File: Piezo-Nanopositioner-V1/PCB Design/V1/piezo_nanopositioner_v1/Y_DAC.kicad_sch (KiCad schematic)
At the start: 29 parts, among them J6 Conn_01x10_Pin, J7 RF2-04A-T-00-50-G, U7 TL431AIDBZR, U8 DAC0800LCM, U9 TDA2050

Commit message: started PCB design, almost finished first DAC.
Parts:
- removed J7: RF2-04A-T-00-50-G, RF:CONN_RF2-04A-T-00-50-G_ADM, symbol SMA_Connector:RF2-04A-T-00-50-G
- added J3: RF2-04A-T-00-50-G, CONN_RF2-04A-T-00-50-G_ADM, symbol SMA_Connector:RF2-04A-T-00-50-G
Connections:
- net at C29.2, R38.2, R39.1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: now also J3.1 (Sig)
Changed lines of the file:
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@@
-	)
-	(symbol
-		(lib_id "SMA_Connector:RF2-04A-T-00-50-G")
-		(at 224.79 101.6 0)
-		(unit 1)
-		(exclude_from_sim no)
-		(in_bom yes)
-		(on_board yes)
-		(dnp no)
-		(fields_autoplaced yes)
-		(property "Reference" "J7"
-			(at 238.76 100.3299 0)
-			(effects
-				(font
-					(size 1.524 1.524)
-				)
-				(justify left)
-			)
-		)
-		(property "Value" "RF2-04A-T-00-50-G"
-			(at 238.76 102.8699 0)
-			(effects
-				(font
-					(size 1.524 1.524)
-				)
-				(justify left)
-			)
-		)
-		(property "Footprint" "RF:CONN_RF2-04A-T-00-50-G_ADM"
-			(at 224.79 101.6 0)
-			(effects
-				(font
-					(size 1.27 1.27)
-					(italic yes)
-				)
-				(hide yes)
-			)
-		)
-		(property "Datasheet" "RF2-04A-T-00-50-G"
-			(at 224.79 101.6 0)
-			(effects
-				(font
-					(size 1.27 1.27)
-					(italic yes)
-				)
-				(hide yes)
-			)
-		)
-		(property "Description" ""
-			(at 224.79 101.6 0)
-			(effects
-				(font
-					(size 1.27 1.27)
-				)
-				(hide yes)
-			)
-		)
-		(pin "1"
-		)
-		(instances
-			(project "piezo_nanopositioner_v1"
-				(path "/7b2a32d8-cc7d-471d-a8eb-eea62713ed45/2b7af091-9ff3-4afc-ada8-05e74516fa9c"
-					(reference "J7")
-					(unit 1)
-				)
-			)
-		)
 	)
 	(symbol
@@
 					(unit 1)
 				)
+			)
+		)
+	)
+	(symbol
+		(lib_id "SMA_Connector:RF2-04A-T-00-50-G")
+		(at 224.79 101.6 0)
+		(unit 1)
+		(exclude_from_sim no)
+		(in_bom yes)
+		(on_board yes)
+		(dnp no)
+		(fields_autoplaced yes)
+		(property "Reference" "J3"
+			(at 238.76 100.3299 0)
+			(effects
+				(font
+					(size 1.524 1.524)
+				)
+				(justify left)
+			)
+		)
+		(property "Value" "RF2-04A-T-00-50-G"
+			(at 238.76 102.8699 0)
+			(effects
+				(font
+					(size 1.524 1.524)
+				)
+				(justify left)
+			)
+		)
+		(property "Footprint" "CONN_RF2-04A-T-00-50-G_ADM"
+			(at 225.552 92.456 0)
+			(effects
+				(font
+					(size 1.27 1.27)
+					(italic yes)
+				)
+				(hide yes)
+			)
+		)
+		(property "Datasheet" "RF2-04A-T-00-50-G"
+			(at 217.17 104.394 0)
+			(effects
+				(font
+					(size 1.27 1.27)
+					(italic yes)
+				)
+				(hide yes)
+			)
+		)
+		(property "Description" ""
+			(at 224.79 101.6 0)
+			(effects
+				(font
+					(size 1.27 1.27)
+				)
+				(hide yes)
+			)
+		)
+		(pin "1"
+		)
+		(instances
+			(project "piezo_nanopositioner_v1"
+				(path "/7b2a32d8-cc7d-471d-a8eb-eea62713ed45/2b7af091-9ff3-4afc-ada8-05e74516fa9c"
+					(reference "J3")
+					(unit 1)
+				)

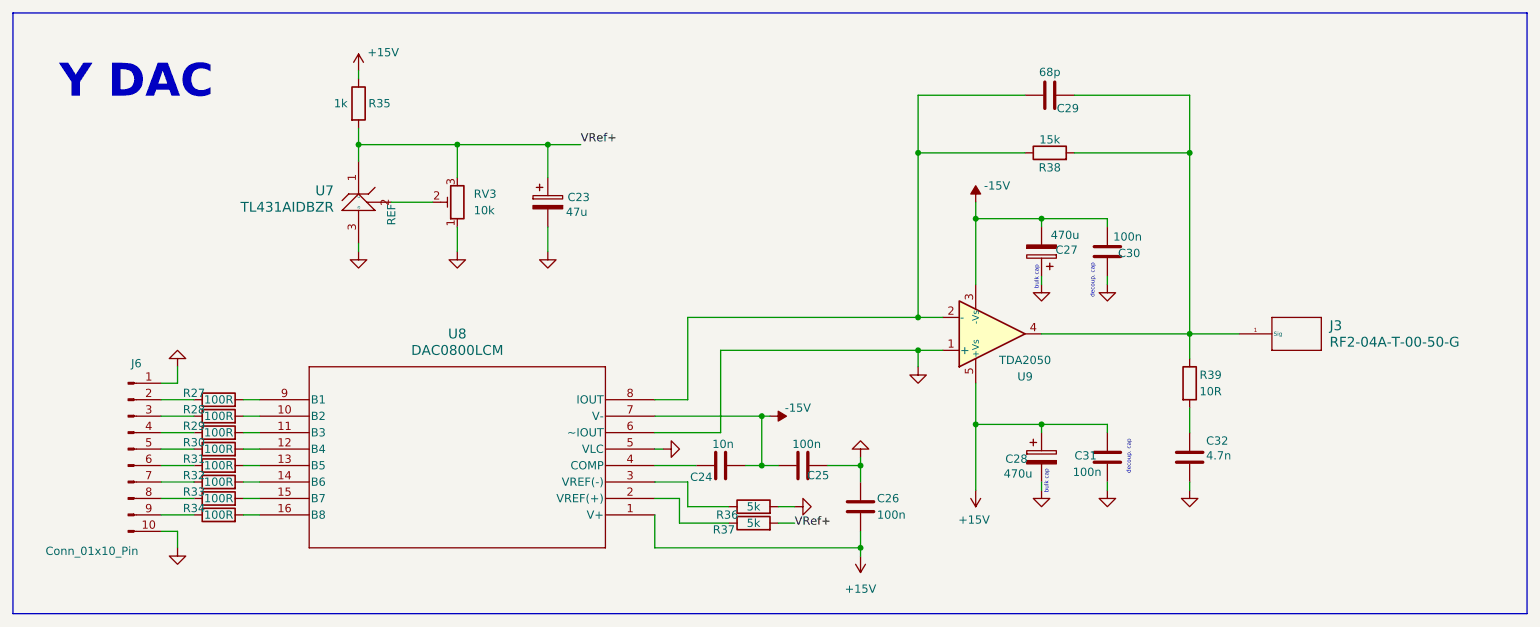
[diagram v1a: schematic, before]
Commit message: Created rough PCB component layout for Z actuator.
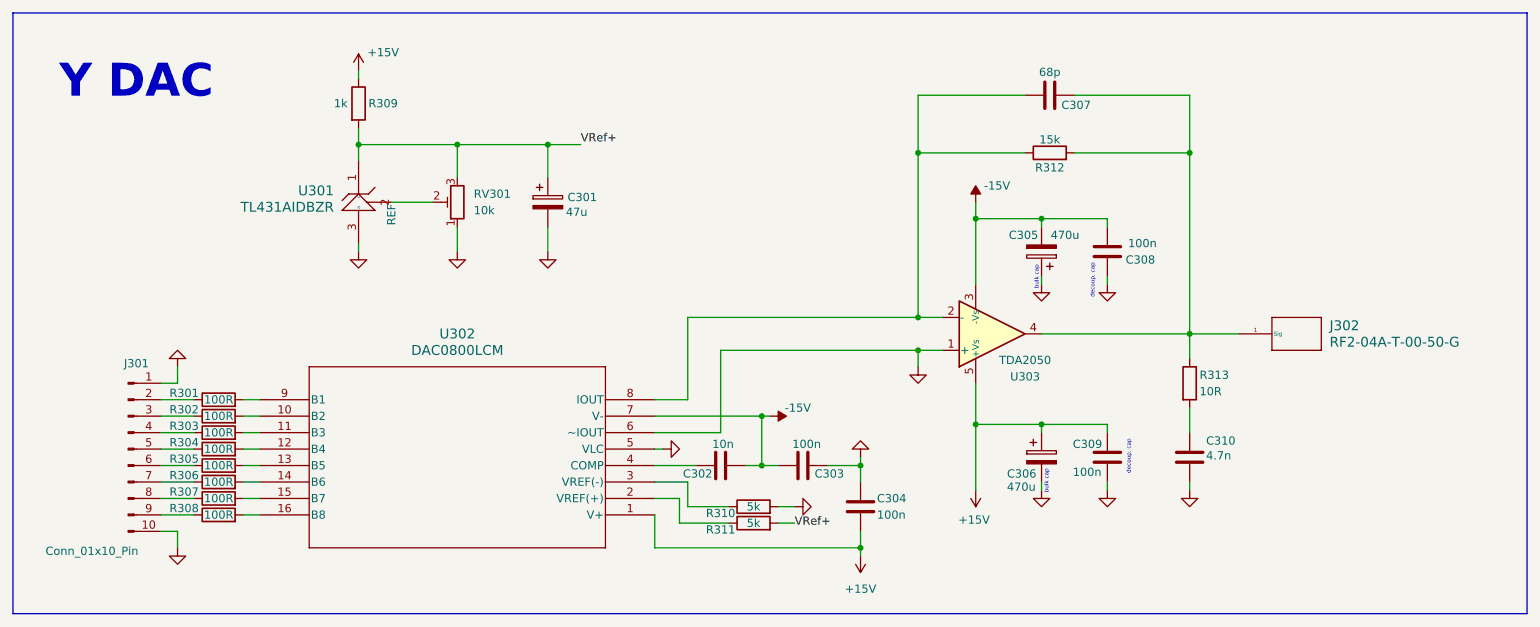
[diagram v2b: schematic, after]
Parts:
- renumbered C23 to C301, C24 to C302, C25 to C303, C26 to C304, C27 to C305, C28 to C306, C29 to C307, C30 to C308, C31 to C309, C32 to C310, J6 to J301, J3 to J302, R27 to R301, R28 to R302, R29 to R303, R30 to R304, R31 to R305, R32 to R306, R33 to R307, R34 to R308, R35 to R309, R36 to R310, R37 to R311, R38 to R312, R39 to R313, RV3 to RV301, U7 to U301, U8 to U302, U9 to U303

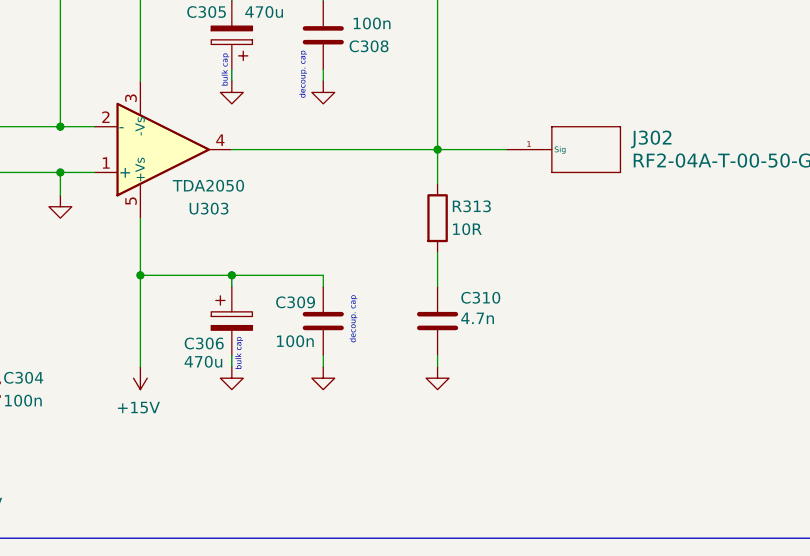
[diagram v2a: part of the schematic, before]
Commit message: added heatsink to XYZ schematics, finalized BOM, minimal PCB layout done.
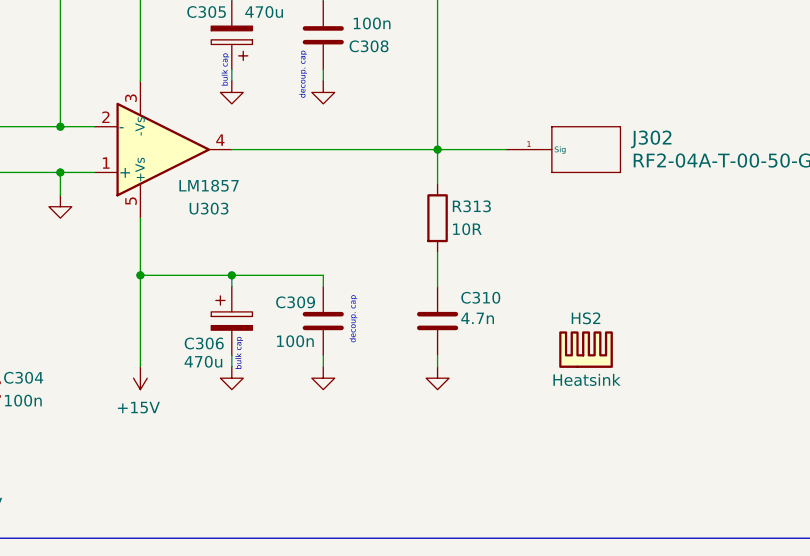
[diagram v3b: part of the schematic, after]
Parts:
- added HS2: Heatsink, V6560Y:V6560Y, symbol Mechanical:Heatsink
- C301: Distributor Link (none) -> https://www.digikey.ca/en/products/detail/panasonic-electro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; Manufacturer (none) -> Panasonic Electronic Components; Manufacturer Part (none) -> EEE-FC1E470P
- C302: Distributor Link (none) -> https://www.digikey.ca/en/products/detail/kemet/C0805C103F5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; Manufacturer (none) -> KEMET; Manufacturer Part (none) -> C0805C103F5GECAUTO
- C303, C304, C308, C309: Distributor Link (none) -> https://www.digikey.ca/en/products/detail/kemet/C0805C104K5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; Manufacturer (none) -> KEMET; Manufacturer Part (none) -> C0805C104K5RACTU
- C305, C306: Distributor Link (none) -> https://www.digikey.ca/en/products/detail/panasonic-electro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; Manufacturer (none) -> Panasonic Electronic Components; Manufacturer Part (none) -> EEH-ZS1E471P
- C307: Distributor Link (none) -> https://www.digikey.ca/en/products/detail/kemet/C0805C680K5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; Manufacturer (none) -> KEMET; Manufacturer Part (none) -> C0805C680K5GACTU
- C310: Distributor Link (none) -> https://www.digikey.ca/en/products/detail/kemet/C0805C472KD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; Manufacturer (none) -> KEMET; Manufacturer Part (none) -> C0805C472KDRACAUTO
- J301: Distributor Link (none) -> https://www.digikey.ca/en/products/detail/harwin-inc/M22-25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; Manufacturer (none) -> Harwin Inc.; Manufacturer Part (none) -> M22-2511005
- J302: Distributor Link (none) -> https://www.digikey.ca/en/products/detail/adam-tech/RF2-04A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; Manufacturer (none) -> Adam Tech; Manufacturer Part (none) -> RF2-04A-T-00-50-G
- R301, R302, R303, R304, R305, R306, R307, R308: Distributor Link (none) -> https://www.digikey.ca/en/products/detail/vishay-dale/CRCW0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; Manufacturer (none) -> Vishay Dale; Manufacturer Part (none) -> CRCW0805100RJNEC
- R309: Distributor Link (none) -> https://www.digikey.ca/en/products/detail/bourns-inc/CR0805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; Manufacturer (none) -> Bourns Inc.; Manufacturer Part (none) -> CR0805-JW-102ELF
- R310, R311: Distributor Link (none) -> https://www.digikey.ca/en/products/detail/te-connectivity-p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; Manufacturer (none) -> TE Connectivity Passive Product; Manufacturer Part (none) -> RLC73K2A1R0FTD
- R312: Distributor Link (none) -> https://www.digikey.ca/en/products/detail/rohm-semiconducto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; Manufacturer (none) -> Rohm Semiconductor; Manufacturer Part (none) -> ESR10EZPJ153
- R313: Distributor Link (none) -> https://www.digikey.ca/en/products/detail/bourns-inc/CR0805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; Manufacturer (none) -> Bourns Inc.; Manufacturer Part (none) -> CR0805AFX-10R0EAS
- RV301: Distributor Link (none) -> https://www.digikey.ca/en/products/detail/sparkfun-electron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; Manufacturer (none) -> SparkFun Electronics; Manufacturer Part (none) -> COM-09806
- U301: Distributor Link (none) -> https://www.digikey.ca/en/products/detail/texas-instruments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; Manufacturer (none) -> Texas Instruments; Manufacturer Part (none) -> TL431AIDBZR
- U302: Distributor Link (none) -> https://www.digikey.ca/en/products/detail/texas-instruments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; Manufacturer (none) -> Texas Instruments; Manufacturer Part (none) -> DAC0800LCM/NOPB
- U303: value TDA2050 -> LM1857; Distributor Link (none) -> https://www.digikey.com/en/products/detail/texas-instrument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; Manufacturer (none) -> Texas Instruments; Manufacturer Part (none) -> LM1875T/NOPB
